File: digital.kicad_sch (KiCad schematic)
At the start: 14 parts, among them J8 Conn_01x04_Socket, U7 CNY74-4H

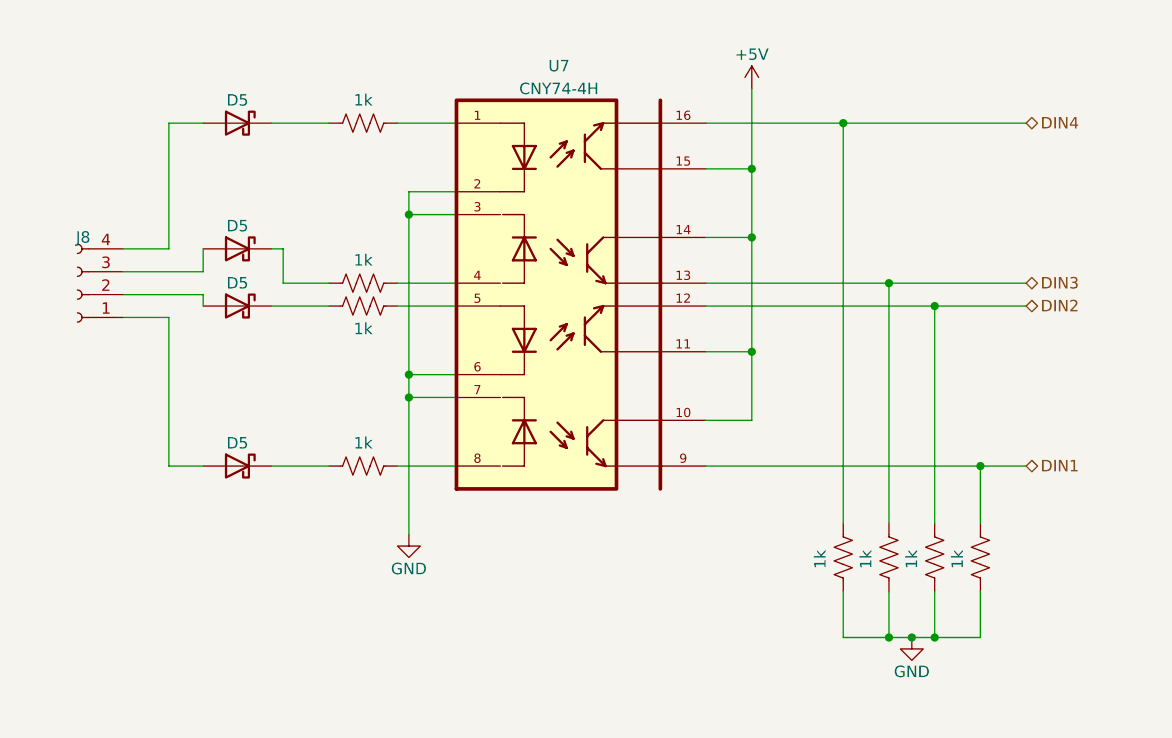
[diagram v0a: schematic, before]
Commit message: Analog input schematic
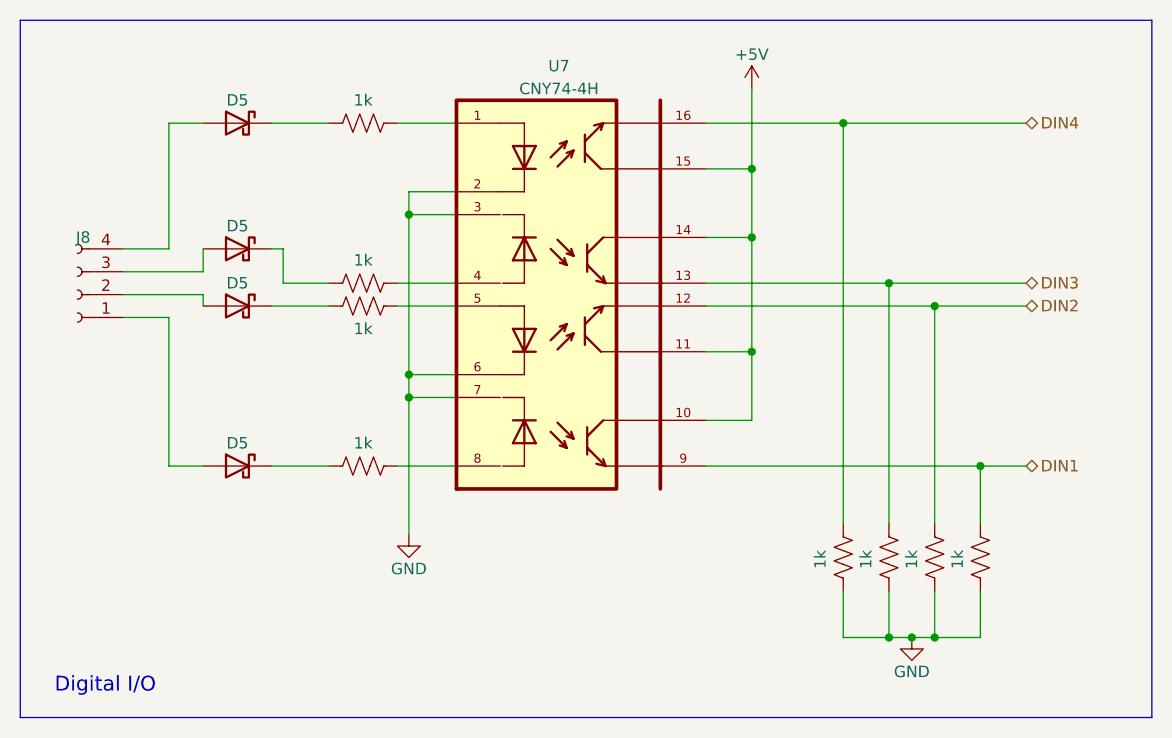
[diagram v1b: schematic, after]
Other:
- note added: "Digital I/O"
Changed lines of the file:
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@@
     (stroke (width 0) (type default))
+  )
+  (rectangle (start 95.25 69.85) (end 220.98 147.32)
+    (stroke (width 0) (type default))
+    (fill (type none))
+  )
+  (text "Digital I/O" (at 99.06 144.78 0)
+    (effects (font (size 1.651 1.651)) (justify left bottom))
   )
   (hierarchical_label "DIN1" (shape bidirectional) (at 207.01 119.38 0) (fields_autoplaced)

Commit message: Schematic of 4-20mA sensor
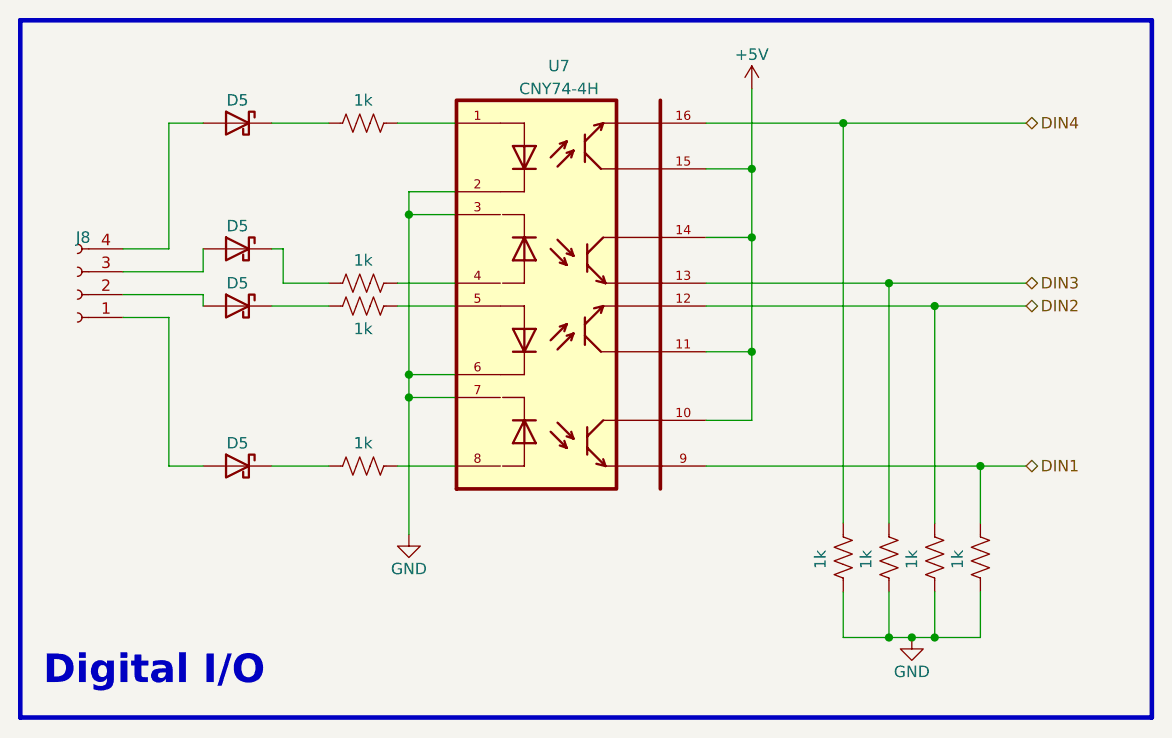
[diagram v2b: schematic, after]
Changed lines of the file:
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@@
   )
   (rectangle (start 95.25 69.85) (end 220.98 147.32)
-    (stroke (width 0) (type default))
+    (stroke (width 0.508) (type default))
     (fill (type none))
   )
-  (text "Digital I/O" (at 99.06 144.78 0)
-    (effects (font (size 1.651 1.651)) (justify left bottom))
+  (text "Digital I/O" (at 97.79 144.018 0)
+    (effects (font (size 3.175 3.175) (thickness 0.635) bold) (justify left bottom))
   )
   (hierarchical_label "DIN1" (shape bidirectional) (at 207.01 119.38 0) (fields_autoplaced)
